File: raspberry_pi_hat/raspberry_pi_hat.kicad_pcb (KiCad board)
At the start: 2 copper layers, 14 parts, among them IC1 LM3940IT, J1 GPIO, J5 LCD_screeen, J6 GPIO, J7 Switches, J8 LED_status, U3 NRF24L01P

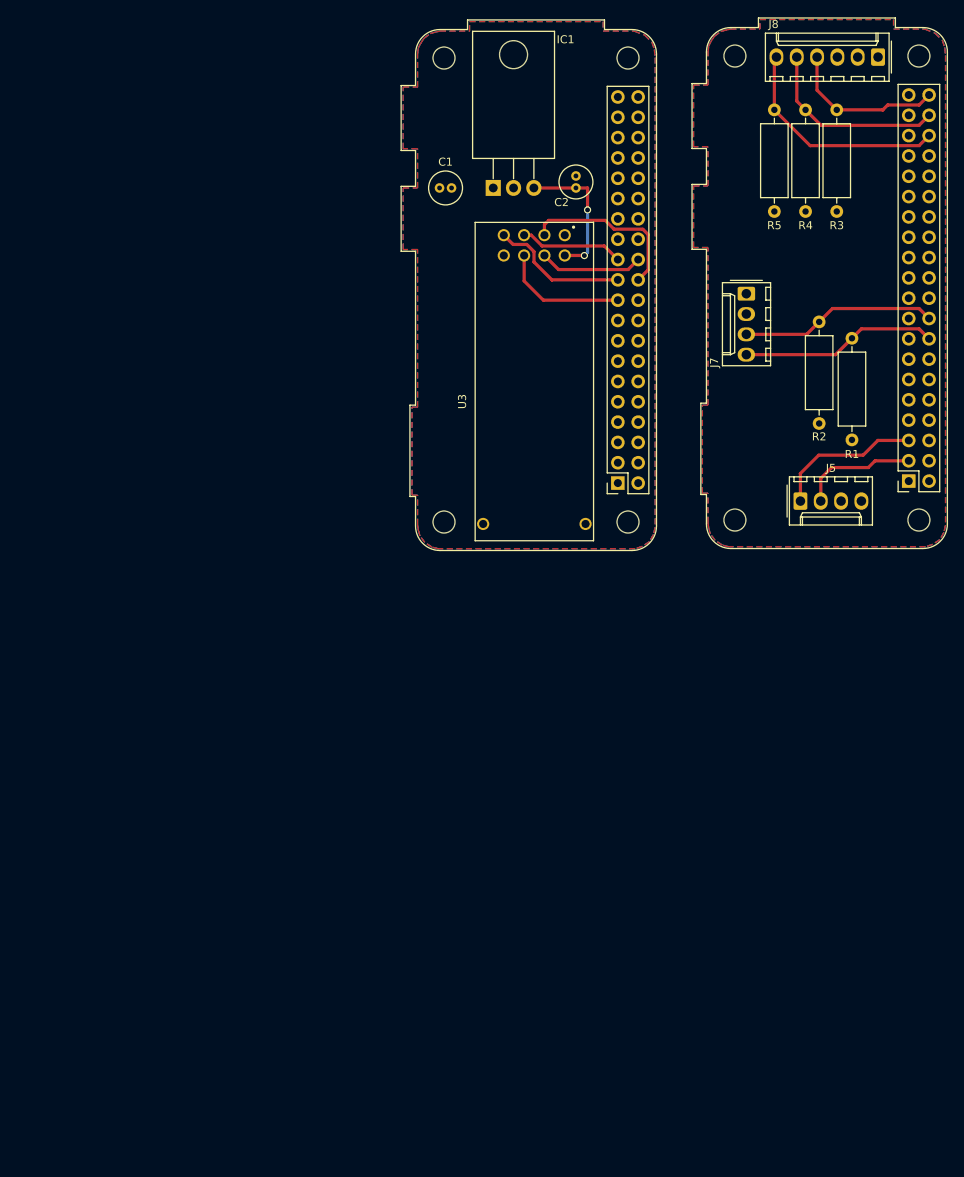
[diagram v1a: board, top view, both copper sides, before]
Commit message: Solved split connection issues between boards
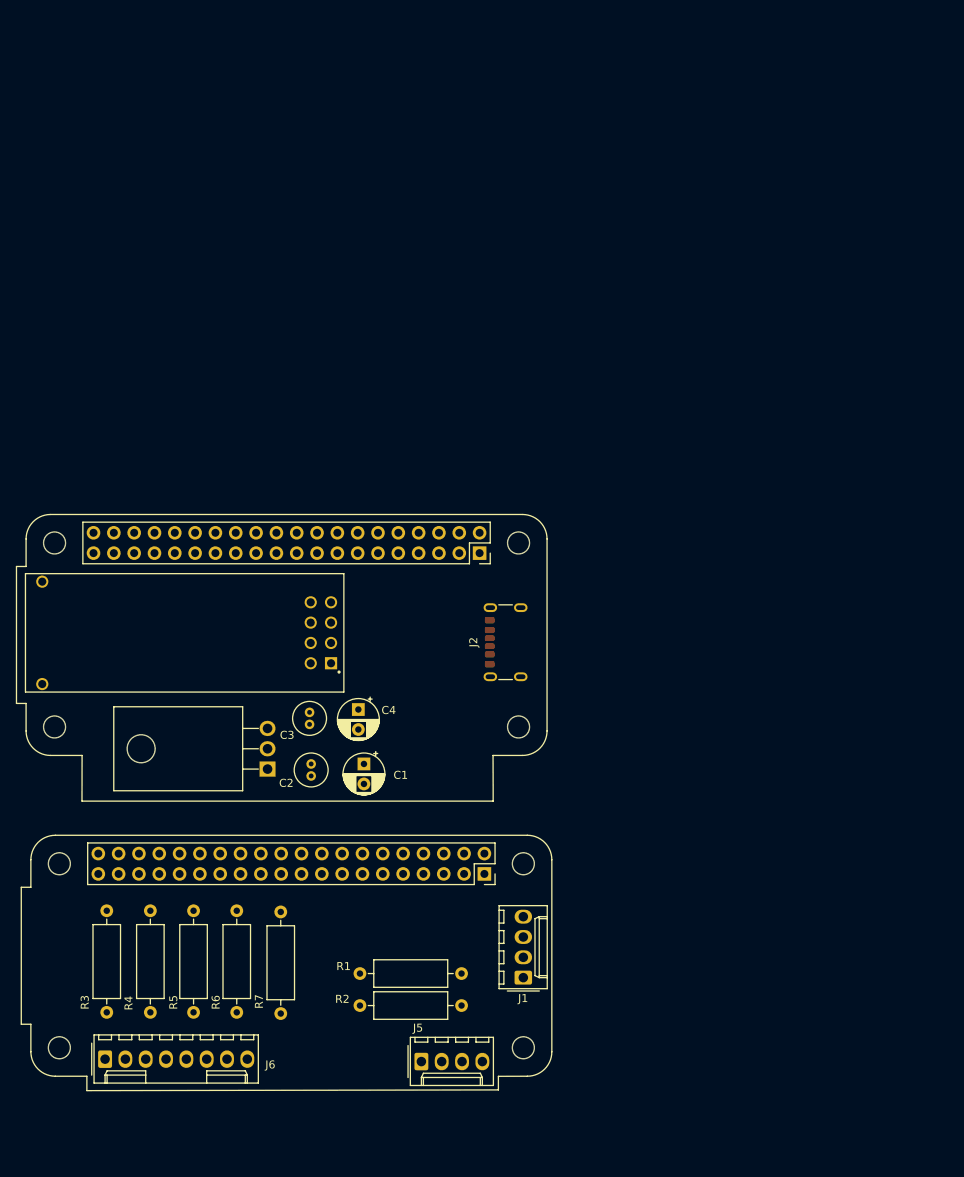
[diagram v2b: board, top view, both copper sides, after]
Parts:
- removed IC1: LM3940IT, Package_TO_SOT_THT:TO-220-3_Horizontal_TabDown
- removed J7: Switches, Connector_Molex:Molex_KK-254_AE-6410-04A_1x04_P2.54mm_Vertical
- removed J8: LED_status, Connector_Molex:Molex_KK-254_AE-6410-06A_1x06_P2.54mm_Vertical
- removed U3: NRF24L01P, NRF24L01P-MODULE-PCB:XCVR_NRF24L01P-MODULE-PCB
- added C3: 33uF, Capacitor_THT:C_Radial_D4.0mm_H5.0mm_P1.50mm, F.Cu at (124.0, 144.1)
- added C4: 10uF, Capacitor_THT:CP_Radial_D5.0mm_P2.50mm, F.Cu at (130.1, 143.7)
- added IC2: LM3940IT, Package_TO_SOT_THT:TO-220F-3_Horizontal_TabDown, F.Cu at (118.8, 151.1)
- added J2: USB_C_Power, Connector_USB:USB_C_Receptacle_GCT_USB4125-xx-x-0190_6P_TopMnt_Horizontal, F.Cu at (149.6, 135.3)
- added J3: GPIO, Module:Raspberry_Pi_Zero_Socketed_THT_FaceDown_MountingHoles, F.Cu at (145.3, 124.1)
- added J4: GPIO, Module:Raspberry_Pi_Zero_Socketed_THT_FaceDown_MountingHoles, F.Cu at (145.9, 164.2)
- added R6: 220, Resistor_THT:R_Axial_DIN0309_L9.0mm_D3.2mm_P12.70mm_Horizontal, F.Cu at (114.9, 181.6)
- added R7: 220, Resistor_THT:R_Axial_DIN0309_L9.0mm_D3.2mm_P12.70mm_Horizontal, F.Cu at (120.4, 181.7)
- added U1: NRF24L01P, NRF24L01P-MODULE-PCB:XCVR_NRF24L01P-MODULE-PCB, F.Cu at (128.8, 126.2)
- C1: value 0,47uF -> 10uF; footprint Capacitor_THT:C_Radial_D4.0mm_H5.0mm_P1.50mm -> Capacitor_THT:CP_Radial_D5.0mm_P2.50mm
- C2: value 33uF -> 0,47uF
- J1: value GPIO -> LCD_screeen; footprint Module:Raspberry_Pi_Zero_Socketed_THT_FaceDown_MountingHoles -> Connector_Molex:Molex_KK-254_AE-6410-04A_1x04_P2.54mm_Vertical
- J5: value LCD_screeen -> Switches
- J6: value GPIO -> LED_status; footprint Module:Raspberry_Pi_Zero_Socketed_THT_FaceDown_MountingHoles -> Connector_Molex:Molex_KK-254_AE-6410-08A_1x08_P2.54mm_Vertical
- moved R3 135.5 mm to (98.7, 181.6)
- moved R4 129.3 mm to (104.1, 181.6)
- moved J6 123.7 mm to (98.4, 187.4), turned to 0 degrees
- moved R5 123.7 mm to (109.5, 181.6)
- moved R2 92.7 mm to (130.3, 180.7), turned to 0 degrees
- moved R1 90.7 mm to (130.3, 176.7), turned to 0 degrees
- moved J5 84.6 mm to (138.0, 187.7)
- moved C2 79.2 mm to (124.2, 150.5), turned to -90 degrees
- moved C1 72.6 mm to (130.8, 150.5), turned to -90 degrees
- moved J1 62.9 mm to (150.7, 177.2), turned to 90 degrees
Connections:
- C2 pad 1: +3V3 -> +5V
- J1 pad 1: unconnected-(J1-Pin_1-Pad1) -> /interface/GPIO3/SCL1
- J1 pad 2: +5V -> /interface/GPIO2/SDA1
- J1 pad 3: /GPIO2/SDA1 -> GND1
- J1 pad 4: +5V -> +5VA
- J5 pad 1: /GPIO3/SCL1 -> GND1
- J5 pad 2: /GPIO2/SDA1 -> GND1
- J5 pad 3: GND -> /interface/GPIO24
- J5 pad 4: +5V -> /interface/GPIO23
- J6 pad 1: unconnected-(J6-Pin_1-Pad1) -> GND1
- J6 pad 2: +5V -> GND1
- J6 pad 3: /GPIO2/SDA1 -> GND1
- J6 pad 4: +5V -> /interface/GPIO21/PCM.DOUT
- J6 pad 5: /GPIO3/SCL1 -> /interface/GPIO20/PCM.DIN
- J6 pad 6: GND -> /interface/GPIO16
- J6 pad 7: /GPIO4/GPCLK0 -> /interface/GPIO12/PWM0
- J6 pad 8: /GPIO14/TXD0 -> /interface/GPIO7/SPI0.CE1
- R1 pad 1: +5V -> +5VA
- R1 pad 2: /GPIO23 -> /interface/GPIO23
- R2 pad 1: +5V -> +5VA
- R2 pad 2: /GPIO24 -> /interface/GPIO24
- R3 pad 1: +5V -> +5VA
- R3 pad 2: /GPIO21/PCM.DOUT -> /interface/GPIO21/PCM.DOUT
- R4 pad 1: +5V -> +5VA
- R4 pad 2: /GPIO20/PCM.DIN -> /interface/GPIO20/PCM.DIN
- R5 pad 1: +5V -> +5VA
- R5 pad 2: /GPIO16 -> /interface/GPIO16
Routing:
- net /GPIO16: track 28.4 -> 0.00 mm
- net /GPIO23: track 24.7 -> 0.00 mm
- net /GPIO24: track 24.7 -> 0.00 mm
- net /GPIO20/PCM.DIN: track 23.8 -> 0.00 mm
- net CE: track 21.4 -> 0.00 mm
- net /GPIO21/PCM.DOUT: track 19.9 -> 0.00 mm
- net /GPIO3/SCL1: track 18.7 -> 0.00 mm
- net +3V3: track 17.8 -> 0.00 mm, vias 2 -> 0
- net /GPIO9/SPI0.MISO: track 17.3 -> 0.00 mm
- net /GPIO10/SPI0.MOSI: track 15.9 -> 0.00 mm
- net /GPIO2/SDA1: track 14.8 -> 0.00 mm
- net /GPIO11/SPI0.SCLK: track 13.0 -> 0.00 mm
- net CSN: track 13.0 -> 0.00 mm
- removed copper zone on F.Cu, net +5V
- removed copper zone on B.Cu, net GND

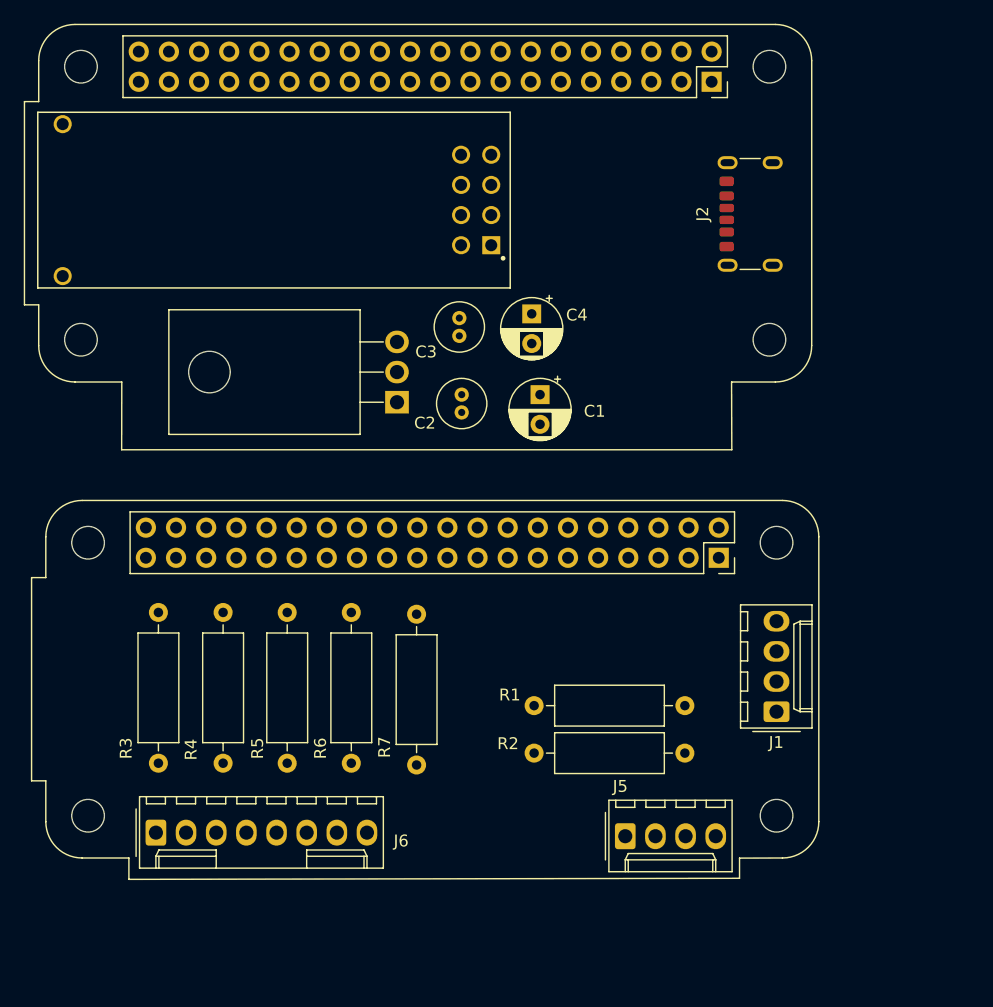
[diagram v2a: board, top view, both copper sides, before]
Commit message: Solved connection issues and THT routing
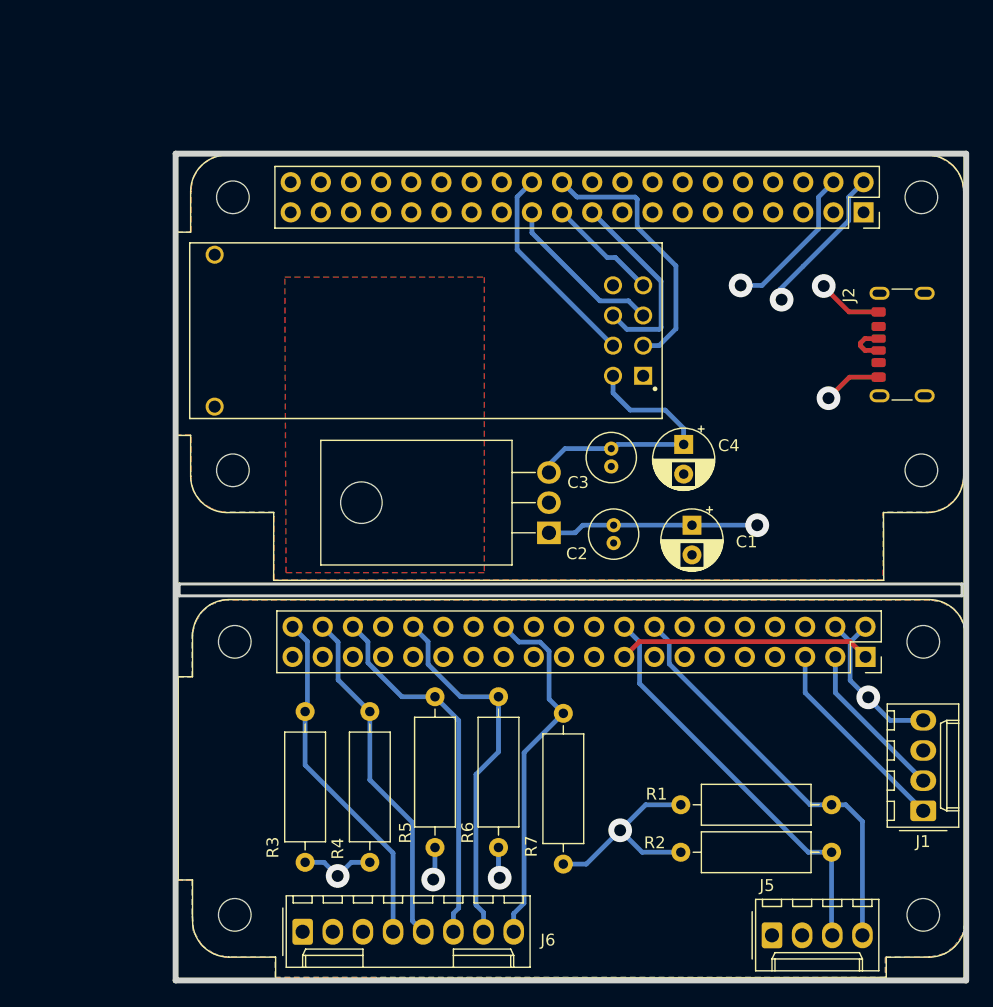
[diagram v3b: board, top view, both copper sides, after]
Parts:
- moved J3 16.9 mm to (158.1, 135.1)
- moved C3 16.9 mm to (136.8, 155.1)
- moved C4 16.9 mm to (142.9, 154.7)
- moved IC2 16.9 mm to (131.6, 162.1)
- moved J2 16.9 mm to (162.4, 146.3)
- moved U1 16.9 mm to (141.6, 137.2)
- moved C2 16.9 mm to (137.0, 161.5)
- moved C1 16.9 mm to (143.6, 161.5)
- moved J5 14.9 mm to (150.3, 196.1)
- moved J1 14.9 mm to (163.1, 185.6)
- moved J4 14.9 mm to (158.2, 172.6)
- moved R1 14.9 mm to (142.7, 185.1)
- moved R2 14.9 mm to (142.7, 189.1)
- moved R7 14.9 mm to (132.8, 190.1)
- moved J6 14.9 mm to (110.8, 195.8)
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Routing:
- net +5VA: track 0.00 -> 44.0 mm, vias 0 -> 5
- net +5V: track 0.00 -> 43.5 mm, vias 0 -> 3
- net /interface/GPIO23: track 0.00 -> 35.0 mm
- net /interface/GPIO24: track 0.00 -> 34.4 mm
- net /interface/GPIO12/PWM0: track 0.00 -> 31.6 mm
- net /interface/GPIO16: track 0.00 -> 31.2 mm
- net /interface/GPIO7/SPI0.CE1: track 0.00 -> 30.5 mm
- net /interface/GPIO21/PCM.DOUT: track 0.00 -> 29.4 mm
- net /interface/GPIO20/PCM.DIN: track 0.00 -> 29.2 mm
- net +3V3: track 0.00 -> 22.7 mm
- net CE: track 0.00 -> 22.5 mm
- net unconnected-(J4-Pin_1-Pad1): track 0.00 -> 21.4 mm
- net CSN: track 0.00 -> 17.6 mm
- net /interface/GPIO3/SCL1: track 0.00 -> 17.1 mm
- net /Transceiver/GPIO10/SPI0.MOSI: track 0.00 -> 16.7 mm
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- added copper zone on F.Cu, net (none)
- added copper zone on F.Cu, net +5V
- added copper zone on F.Cu, net +5VA
- added copper zone on B.Cu, net GND
- added copper zone on B.Cu, net GND1
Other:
- board outline added: 66.6 x 69.7 mm
